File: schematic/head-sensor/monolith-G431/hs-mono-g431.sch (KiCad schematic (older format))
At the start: 42 parts, among them P1 MICROSD-SDIO-CD, P2 SWD, U1 STM32F103RE, Y1 8MHz, Y2 32768Hz

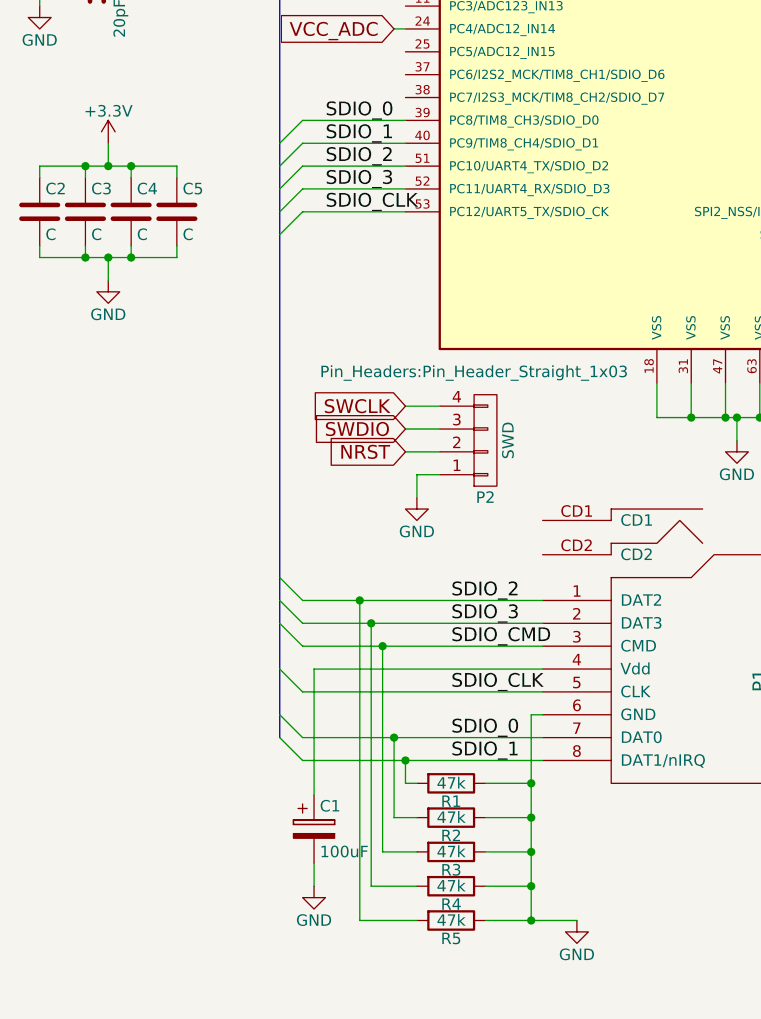
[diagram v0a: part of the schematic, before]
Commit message: [PCB] monolith HS for G431 schematic fixed, NRF24L01 module added for 1100m variant
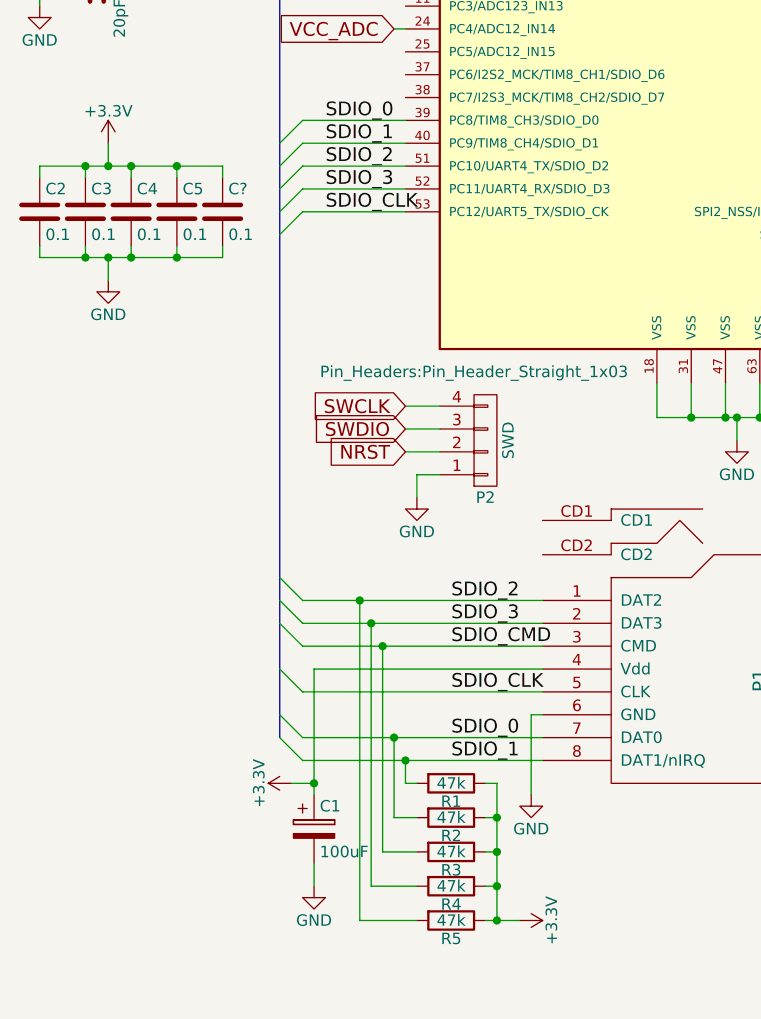
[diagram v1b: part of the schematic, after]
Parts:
- added C?: 0.1, symbol C
- C2, C3, C4, C5: value C -> 0.1
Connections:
- net +3V3: now also C1.1, P1.4 (Vdd), R1.1, R2.1, R3.1, R4.1, R5.1, C?.1
- net GND: now also C?.2; no longer R1.1, R2.1, R3.1, R4.1, R5.1
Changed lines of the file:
@@
 P 800 4350
 F 0 "C2" H 825 4450 50  0000 L CNN
-F 1 "C" H 825 4250 50  0000 L CNN
+F 1 "0.1" H 825 4250 50  0000 L CNN
 F 2 "Capacitors_SMD:C_0805" H 838 4200 50  0001 C CNN
 F 3 "" H 800 4350 50  0000 C CNN
@@
 P 1000 4350
 F 0 "C3" H 1025 4450 50  0000 L CNN
-F 1 "C" H 1025 4250 50  0000 L CNN
+F 1 "0.1" H 1025 4250 50  0000 L CNN
 F 2 "Capacitors_SMD:C_0805" H 1038 4200 50  0001 C CNN
 F 3 "" H 1000 4350 50  0000 C CNN
@@
 P 1200 4350
 F 0 "C4" H 1225 4450 50  0000 L CNN
-F 1 "C" H 1225 4250 50  0000 L CNN
+F 1 "0.1" H 1225 4250 50  0000 L CNN
 F 2 "Capacitors_SMD:C_0805" H 1238 4200 50  0001 C CNN
 F 3 "" H 1200 4350 50  0000 C CNN
@@
 P 1400 4350
 F 0 "C5" H 1425 4450 50  0000 L CNN
-F 1 "C" H 1425 4250 50  0000 L CNN
+F 1 "0.1" H 1425 4250 50  0000 L CNN
 F 2 "Capacitors_SMD:C_0805" H 1438 4200 50  0001 C CNN
 F 3 "" H 1400 4350 50  0000 C CNN
@@
 	1    2600 7450
 	0    1    1    0
-$EndComp
-$Comp
-L GND #PWR05
-U 1 1 57F14910
-P 3150 7450
-F 0 "#PWR05" H 3150 7200 50  0001 C CNN
-F 1 "GND" H 3150 7300 50  0000 C CNN
-F 2 "" H 3150 7450 50  0000 C CNN
-F 3 "" H 3150 7450 50  0000 C CNN
-	1    3150 7450
-	1    0    0    -1
 $EndComp
 $Comp
@@
 	800  4200 800  4150
 Wire Wire Line
-	800  4150 1400 4150
+	800  4150 1600 4150
 Wire Wire Line
 	1400 4150 1400 4200
@@
 	800  4500 800  4550
 Wire Wire Line
-	800  4550 1400 4550
+	800  4550 1600 4550
 Wire Wire Line
 	1400 4550 1400 4500
@@
 Wire Wire Line
 	3000 6550 2950 6550
-Wire Wire Line
-	2950 6550 2950 7450
-Wire Wire Line
-	2750 7450 3150 7450
-Wire Wire Line
-	2750 7300 2950 7300
-Connection ~ 2950 7300
-Wire Wire Line
-	2750 7150 2950 7150
-Connection ~ 2950 7150
-Wire Wire Line
-	2750 7000 2950 7000
-Connection ~ 2950 7000
-Wire Wire Line
-	2750 6850 2950 6850
-Connection ~ 2950 6850
-Connection ~ 2950 7450
 Wire Wire Line
 	2000 6900 2000 6350
@@
 	9450 5500 9450 5100
 Connection ~ 9450 5100
+$Comp
+L C C?
+U 1 1 57F20BF5
+P 1600 4350
+F 0 "C?" H 1625 4450 50  0000 L CNN
+F 1 "0.1" H 1625 4250 50  0000 L CNN
+F 2 "" H 1638 4200 50  0000 C CNN
+F 3 "" H 1600 4350 50  0000 C CNN
+	1    1600 4350
+	1    0    0    -1
+$EndComp
+Wire Wire Line
+	1600 4150 1600 4200
+Connection ~ 1400 4150
+Wire Wire Line
+	1600 4550 1600 4500
+Connection ~ 1400 4550
+$Comp
+L +3.3V #PWR?
+U 1 1 57F21BCF
+P 2900 7450
+F 0 "#PWR?" H 2900 7300 50  0001 C CNN
+F 1 "+3.3V" H 2900 7590 50  0000 C CNN
+F 2 "" H 2900 7450 50  0000 C CNN
+F 3 "" H 2900 7450 50  0000 C CNN
+	1    2900 7450
+	0    1    1    0
+$EndComp
+$Comp
+L +3.3V #PWR?
+U 1 1 57F21D91
+P 1900 6850
+F 0 "#PWR?" H 1900 6700 50  0001 C CNN
+F 1 "+3.3V" H 1900 6990 50  0000 C CNN
+F 2 "" H 1900 6850 50  0000 C CNN
+F 3 "" H 1900 6850 50  0000 C CNN
+	1    1900 6850
+	0    -1   -1   0
+$EndComp
+Wire Wire Line
+	1900 6850 2000 6850
+Connection ~ 2000 6850
+$Comp
+L GND #PWR?
+U 1 1 57F2210D
+P 2950 6900
+F 0 "#PWR?" H 2950 6650 50  0001 C CNN
+F 1 "GND" H 2950 6750 50  0000 C CNN
+F 2 "" H 2950 6900 50  0000 C CNN
+F 3 "" H 2950 6900 50  0000 C CNN
+	1    2950 6900
+	1    0    0    -1
+$EndComp
+Wire Wire Line
+	2750 6850 2800 6850
+Wire Wire Line
+	2800 6850 2800 7450
+Wire Wire Line
+	2750 7450 2900 7450
+Wire Wire Line
+	2750 7300 2800 7300
+Connection ~ 2800 7300
+Wire Wire Line
+	2750 7150 2800 7150
+Connection ~ 2800 7150
+Wire Wire Line
+	2750 7000 2800 7000
+Connection ~ 2800 7000
+Connection ~ 2800 7450
+Wire Wire Line
+	2950 6550 2950 6900
 $EndSCHEMATC

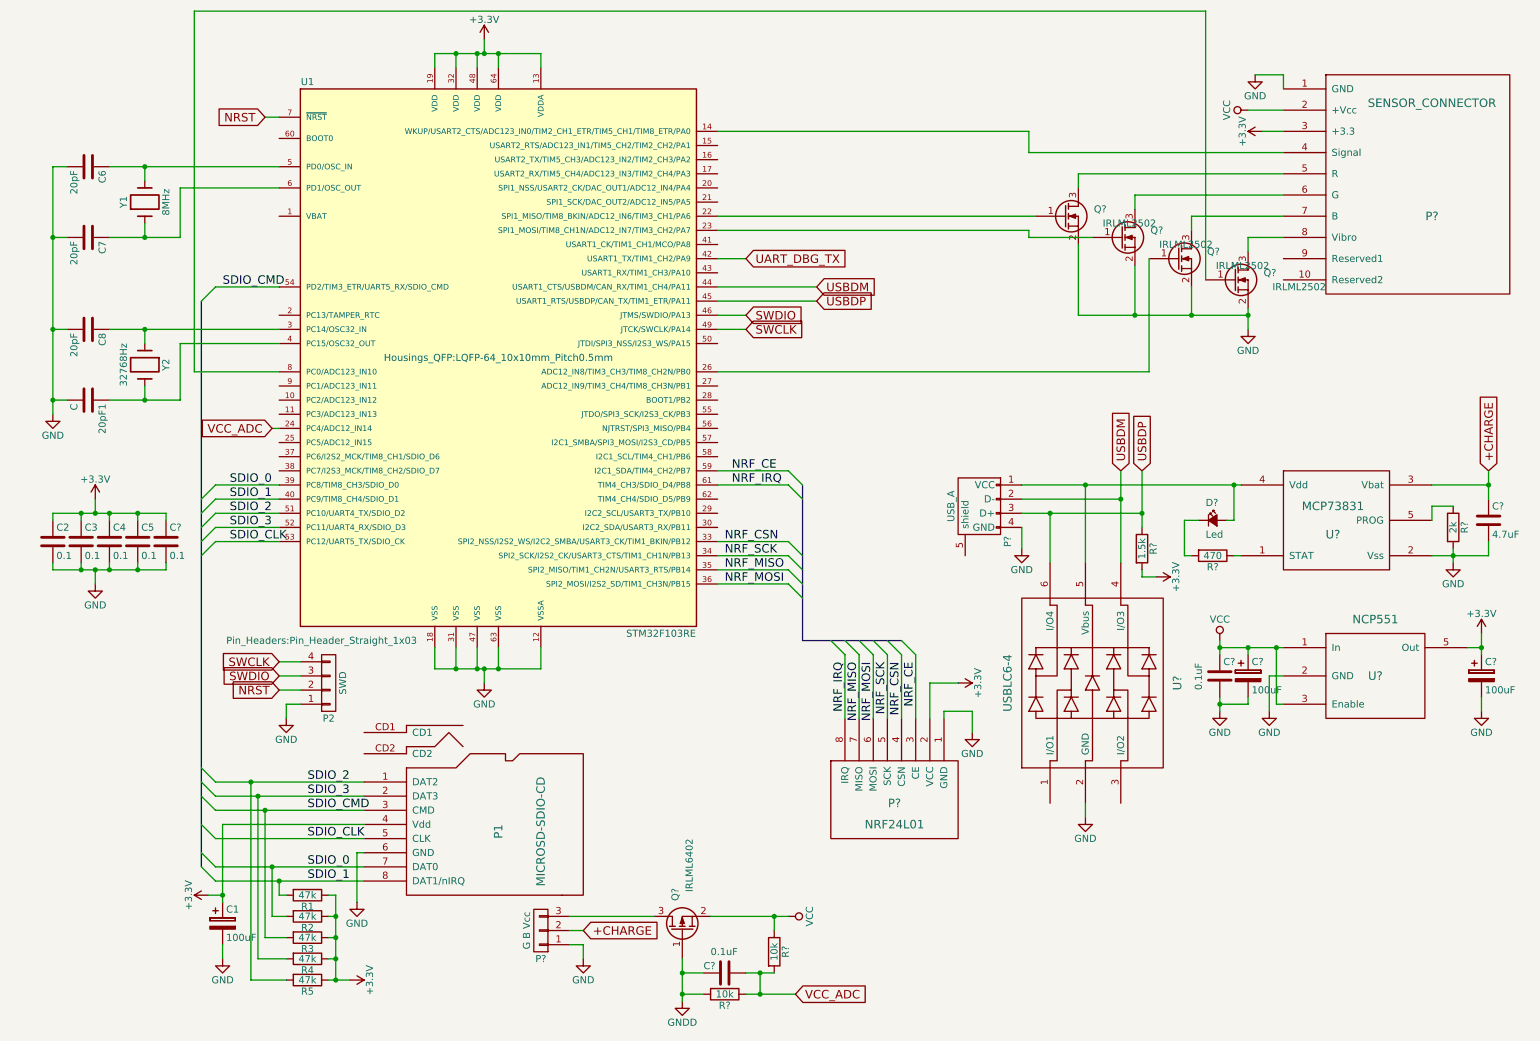
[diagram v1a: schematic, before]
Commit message: [PCB] Monolith HS beginned, initial jobs: board cuts, footprints added to list
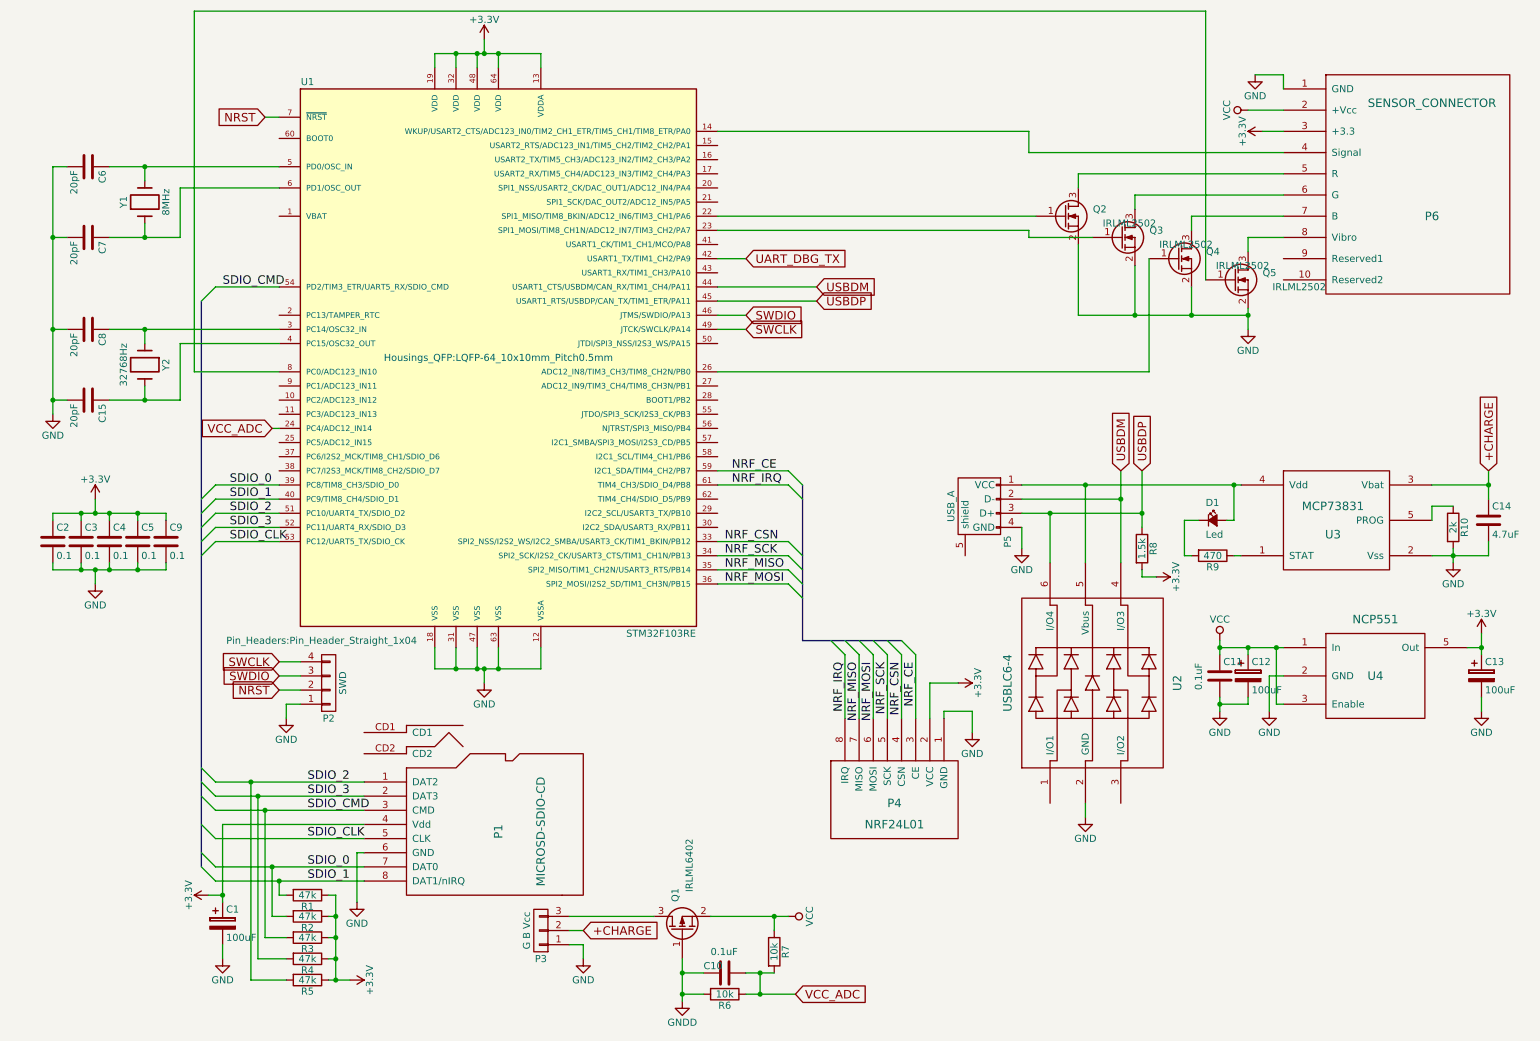
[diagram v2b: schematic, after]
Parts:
- C10, C11, C14, C9: renamed from C?; footprint (none) -> Capacitors_SMD:C_0805
- C12, C13: renamed from C?; footprint (none) -> Capacitors_Tantalum_SMD:TantalC_SizeB_EIA-3528_Reflow
- C15: renamed from 20pF1; value C -> 20pF; footprint (none) -> Capacitors_SMD:C_0805
- C6, C7, C8: footprint (none) -> Capacitors_SMD:C_0805
- D1: renamed from D?; footprint (none) -> LEDs:LED_0805
- P2: footprint Pin_Headers:Pin_Header_Straight_1x03 -> Pin_Headers:Pin_Header_Straight_1x04
- P3: renamed from P?; footprint (none) -> Pin_Headers:Pin_Header_Straight_1x03
- P4: renamed from P?; footprint (none) -> components:NRF25L01-universal
- P5: renamed from P?; footprint (none) -> Connect:USB_B
- P6: renamed from P?; footprint (none) -> Pin_Headers:Pin_Header_Straight_1x08
- Q1, Q2, Q3, Q4, Q5: renamed from Q?; footprint (none) -> TO_SOT_Packages_SMD:SOT-23
- R10, R6, R7, R8, R9: renamed from R?; footprint (none) -> Resistors_SMD:R_0805
- U2: renamed from U?; footprint (none) -> TO_SOT_Packages_SMD:SOT-23-6
- U3, U4: renamed from U?; footprint (none) -> TO_SOT_Packages_SMD:SOT-23-5
- Y1: footprint (none) -> Crystals:Crystal_HC49-U_Vertical
- Y2: footprint (none) -> Crystals:Crystal_Round_Horizontal_3mm

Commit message: [PCB] Monolith head sensor PCB first iteration done. Bluetooth added. Silk not ready
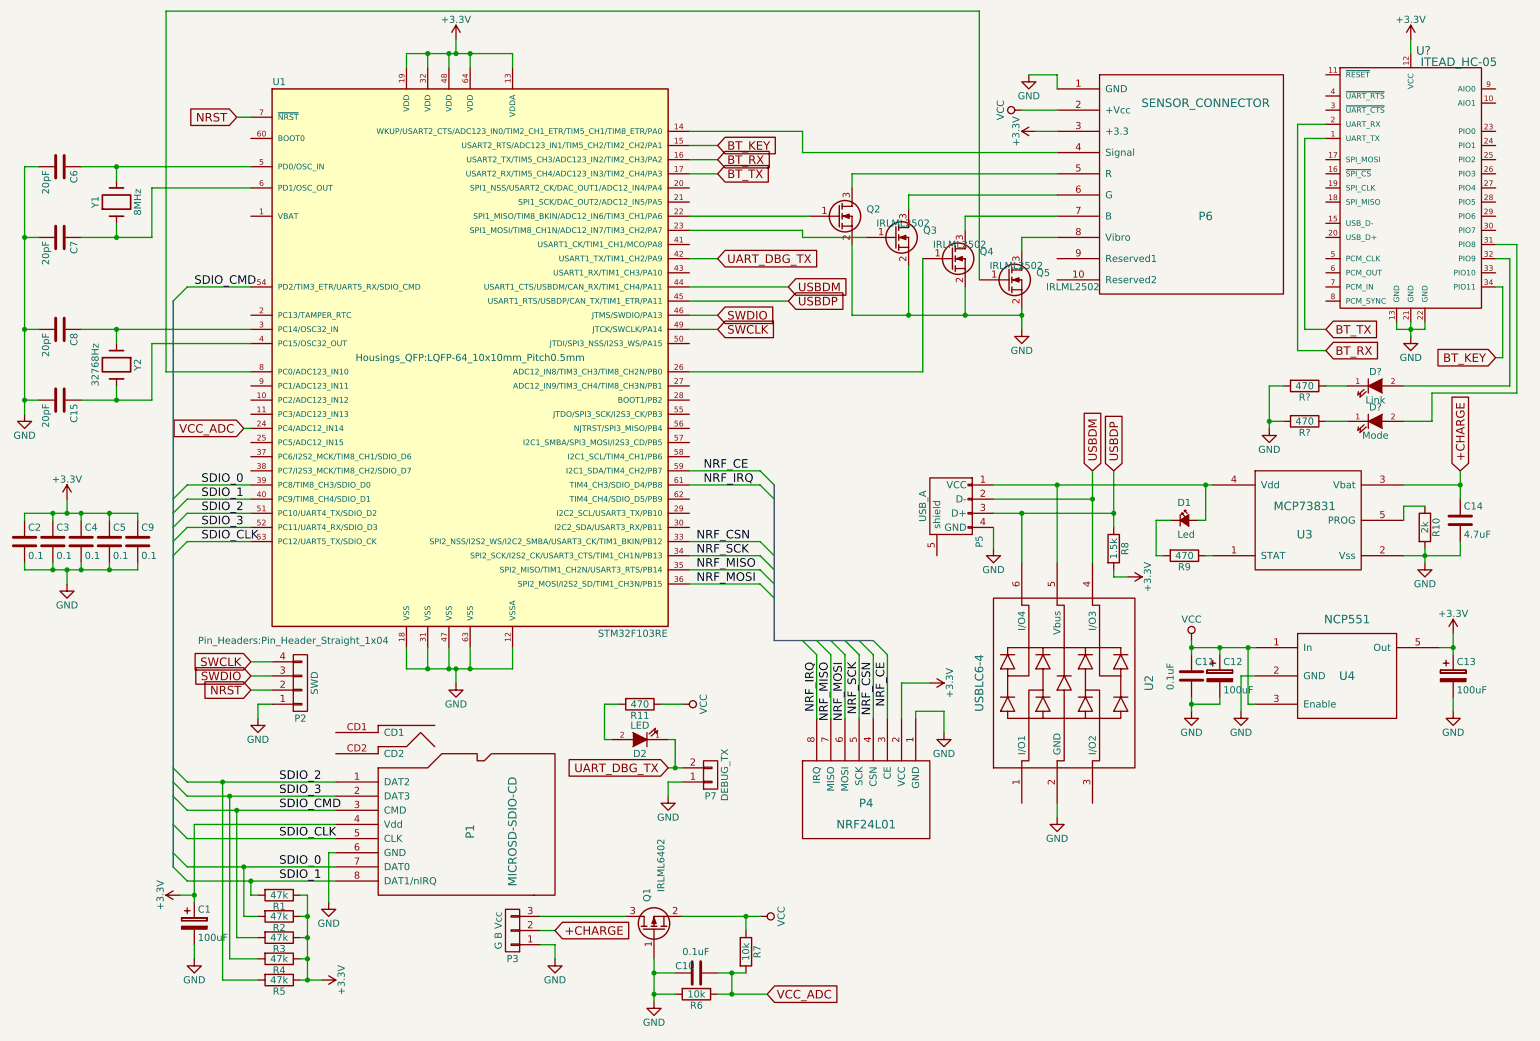
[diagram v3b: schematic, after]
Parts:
- added D2: LED, LEDs:LED_0805, symbol LED
- added D?: Link, symbol LED
- added D?: Mode, symbol LED
- added P7: DEBUG_TX, Pin_Headers:Pin_Header_Straight_1x02, symbol CONN_01X02
- added R11: 470, Resistors_SMD:R_0805, symbol R
- added R? (x2): 470, symbol R
- added U?: ITEAD_HC-05, symbol ITEAD_HC-05
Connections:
- net GNDD is gone; now on net GND: C10.2, Q1.1 (G), R6.2
- net +3V3: now also U?.12 (VCC)
- net GND: now also P7.1 (P1), R?.2, R?.2, U?.13 (GND), U?.21 (GND), U?.22 (GND)
- net UART_DBG_TX: now also D2.1 (K), P7.2 (P2)
- net VCC: now also R11.1
- net BT_KEY: now reaches U1.15 (USART2_RTS/ADC123_IN1/TIM5_CH2/TIM2_CH2/PA1)
- net BT_KEY: now also U?.34 (PIO11)
- net BT_RX: now reaches U1.16 (USART2_TX/TIM5_CH3/ADC123_IN2/TIM2_CH3/PA2)
- net BT_RX: now also U?.2 (UART_RX)
- net BT_TX: now reaches U1.17 (USART2_RX/TIM5_CH4/ADC123_IN3/TIM2_CH4/PA3)
- net BT_TX: now also U?.1 (UART_TX)
- new net: D2.2 (A), R11.2
- new net: D?.2 (A), U?.31 (PIO8)
- new net: D?.2 (A), U?.32 (PIO9)
- new net: D?.1 (K), R?.1 (x2)
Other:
- moved on the sheet: C1, C10, C11, C12, C13, C14, C15, C2, C3, C4, C5, C6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
